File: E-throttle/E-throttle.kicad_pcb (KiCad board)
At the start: 2 copper layers, 100 x 100 mm, 62 parts, among them IC1 BTS441TG, J3 Conn_01x11, J4 Conn_01x11, J5 776087-1, J9 Micro_SD_Card, Q1 NMOS, SW1 SW_Push, U1 74HC123, U2 LM317_SOT-223, U3 LM317_SOT-223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

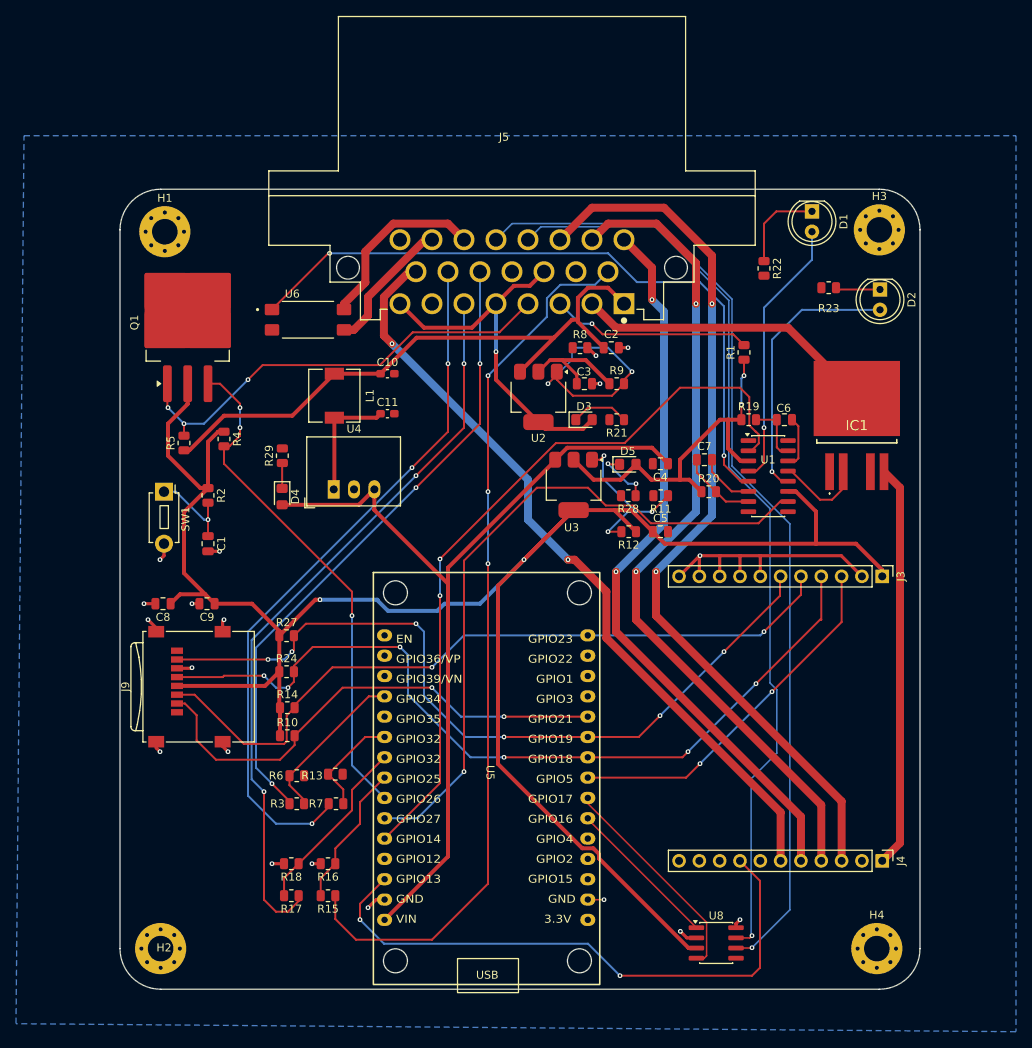
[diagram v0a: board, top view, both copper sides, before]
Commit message: added vias, ran DRC
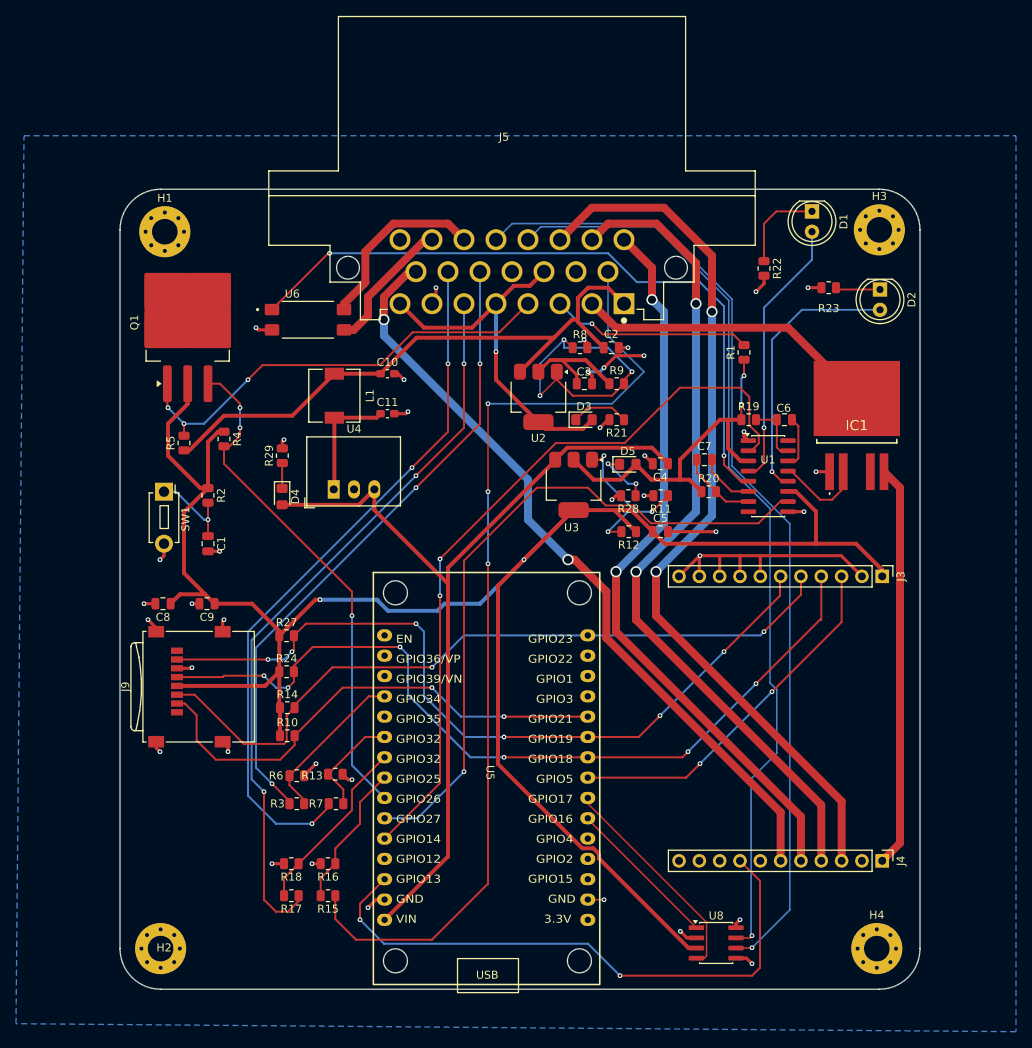
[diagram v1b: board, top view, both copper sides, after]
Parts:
- R13, R16, R18, R6: value 66.5k -> 68k
- R15, R17, R3, R7: value 33.2k -> 33k
- R19: value 10k -> 68k
- R20: value 100k -> 330k
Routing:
- net GND: track 61.9 -> 106.6 mm, vias 18 -> 38
- net /TPS-SIG2: track 111.2 -> 121.5 mm
- net Net-(U2-ADJ): track 29.2 -> 37.1 mm, vias 2 -> 3

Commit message: Added THT filtering capacitors
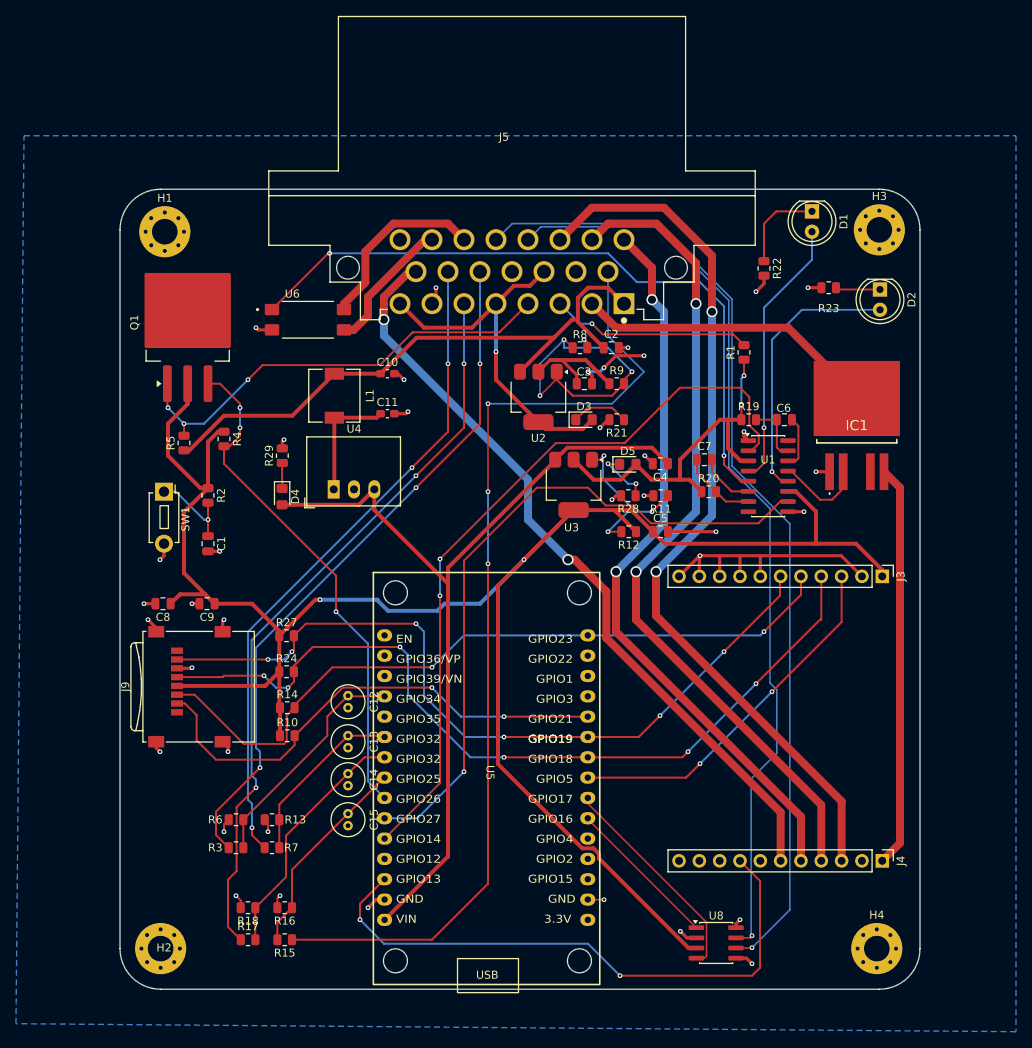
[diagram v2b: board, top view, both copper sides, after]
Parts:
- added C12: 0.1u, Capacitor_THT:C_Radial_D4.0mm_H7.0mm_P1.50mm, F.Cu at (183.2, 96.8)
- added C13: 0.1u, Capacitor_THT:C_Radial_D4.0mm_H7.0mm_P1.50mm, F.Cu at (183.2, 101.8)
- added C14: 0.1u, Capacitor_THT:C_Radial_D4.0mm_H7.0mm_P1.50mm, F.Cu at (183.2, 106.6)
- added C15: 0.1u, Capacitor_THT:C_Radial_D4.0mm_H7.0mm_P1.50mm, F.Cu at (183.2, 111.6)
- R16, R18: value 68k -> 100k
- moved R13 9.75 mm to (173.7, 112.3), turned to 180 degrees
- moved R7 9.71 mm to (173.7, 115.8)
- moved R3 9.38 mm to (169.2, 115.8)
- moved R6 9.38 mm to (169.2, 112.3), turned to 180 degrees
- moved R15 7.72 mm to (175.3, 127.3)
- moved R16 7.72 mm to (175.3, 123.3)
- moved R17 7.72 mm to (170.7, 127.3), turned to 0 degrees
- moved R18 7.72 mm to (170.7, 123.3)
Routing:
- net /APPS-SIG1-OUT: track 20.3 -> 29.0 mm
- net /APPS-SIG2-OUT: track 13.5 -> 22.2 mm
- net /TPS-SIG1-OUT: track 22.5 -> 31.0 mm
- net /TPS-SIG2-OUT: track 18.1 -> 25.8 mm
- net /APPS-SIG1: track 79.8 -> 86.7 mm
- net /APPS-SIG2: track 88.7 -> 83.2 mm
- net /TPS-SIG2: track 121.5 -> 122.9 mm
- net GND: track 106.6 -> 107.3 mm
- net /TPS-SIG1: track 92.3 -> 92.8 mm

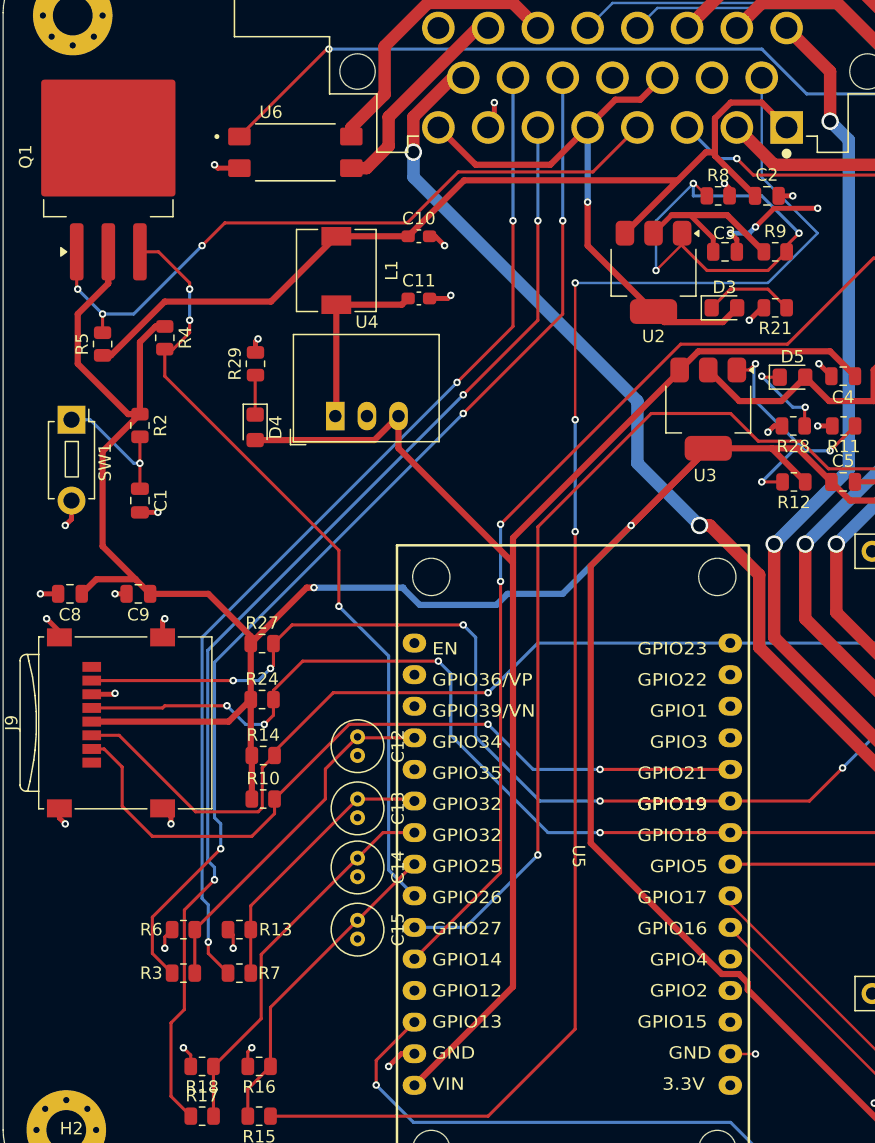
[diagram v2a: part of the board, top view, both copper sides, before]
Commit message: Added FBR Logo
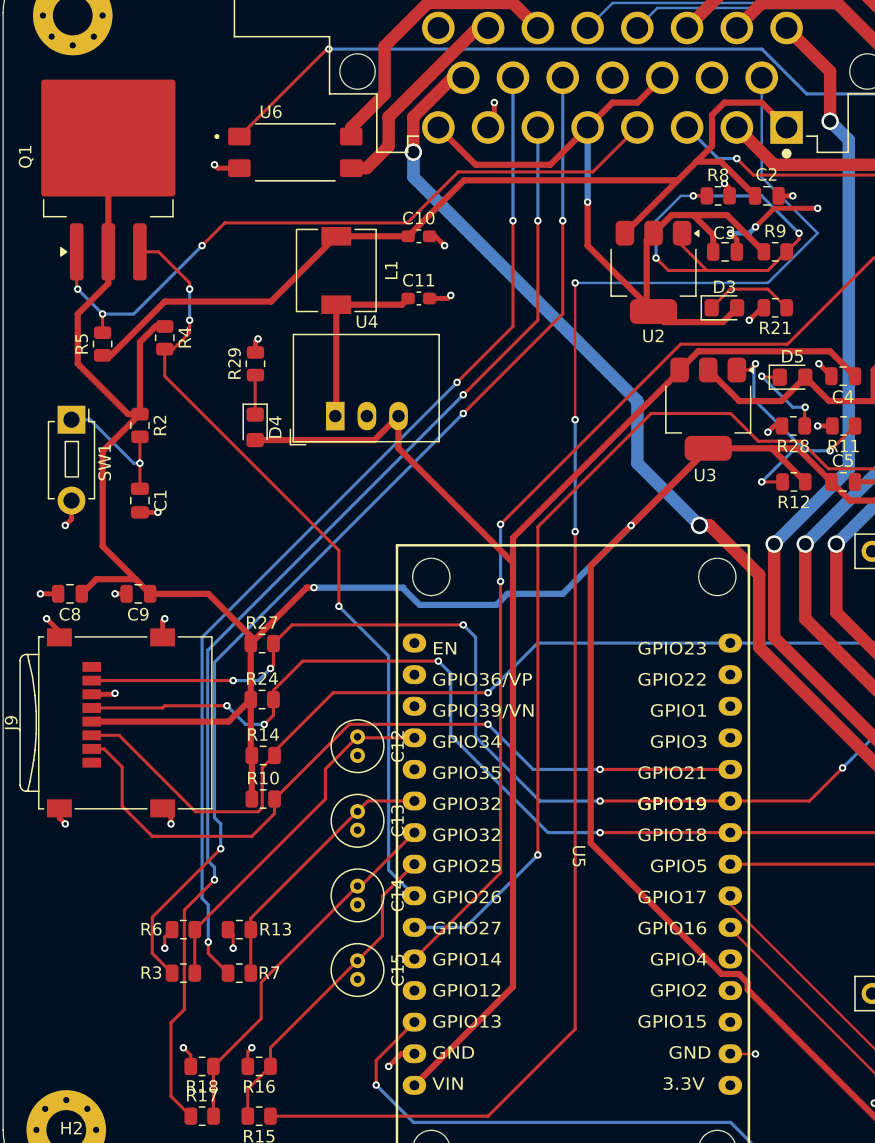
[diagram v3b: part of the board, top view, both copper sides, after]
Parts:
- added E-Throttle (2026): LOGO, FBR_Footprints_additional:FBR_Logo_.9in, B.Cu at (242.5, 60.0)
- moved C15 3.25 mm to (183.2, 114.8)
- moved C14 2.25 mm to (183.2, 108.8)
- moved C13 1.00 mm to (183.2, 102.8)
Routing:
- net +3V3: track 298.8 -> 307.9 mm
- net +5V-SENSORS: track 62.6 -> 67.8 mm
- net Net-(U2-ADJ): track 37.1 -> 35.4 mm
- net /TPS-SIG1-OUT: track 31.0 -> 29.7 mm
- net +12V: track 76.7 -> 77.6 mm

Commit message: Ran DRC - fixed all errors
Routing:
- net GND: track 107.3 -> 111.4 mm, vias 38 -> 39
- net +3V3: track 307.9 -> 310.1 mm
- net /CAN-L: vias 1 -> 3
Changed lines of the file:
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@@
 	)
 	(segment
+		(start 234.76 117.46)
+		(end 232.12 114.82)
+		(width 0.25)
+		(layer "F.Cu")
+		(net 1)
+	)
+	(segment
 		(start 229.68 81.9)
 		(end 229.68 79.36)
@@
 	)
 	(segment
+		(start 232.12 114.82)
+		(end 231.72 114.82)
+		(width 0.25)
+		(layer "F.Cu")
+		(net 1)
+	)
+	(segment
 		(start 221.395 71.82)
 		(end 220.22 71.82)
@@
 	)
 	(via
+		(at 231.72 114.82)
+		(size 0.6)
+		(drill 0.3)
+		(layers "F.Cu" "B.Cu")
+		(net 1)
+	)
+	(via
 		(at 163.72 93.32)
 		(size 0.6)
@@
 	)
 	(segment
+		(start 239.68 71.28)
+		(end 246.22 77.82)
+		(width 0.4)
+		(layer "F.Cu")
+		(net 5)
+	)
+	(segment
 		(start 233.27 67.47)
 		(end 232.295001 67.47)
@@
 	)
 	(segment
-		(start 246.72 77.82)
+		(start 246.22 77.82)
 		(end 241.72 77.82)
 		(width 0.5)
@@
 	)
 	(segment
-		(start 238.22 71.28)
-		(end 239.194999 71.28)
-		(width 0.5)
-		(layer "F.Cu")
-		(net 5)
-	)
-	(segment
 		(start 217.3 69.82)
 		(end 219.22 67.9)
@@
 	)
 	(segment
+		(start 238.22 71.28)
+		(end 239.68 71.28)
+		(width 0.4)
+		(layer "F.Cu")
+		(net 5)
+	)
+	(segment
 		(start 225.795001 128.36)
 		(end 214.59246 117.157459)
@@
 	)
 	(segment
-		(start 241.72 73.805001)
-		(end 241.72 77.82)
-		(width 0.5)
-		(layer "F.Cu")
-		(net 5)
-	)
-	(segment
 		(start 216.52 73.62)
 		(end 219.22 76.32)
@@
 	)
 	(segment
-		(start 239.194999 71.28)
-		(end 241.72 73.805001)
+		(start 246.72 77.82)
+		(end 246.22 77.82)
 		(width 0.5)
 		(layer "F.Cu")
@@
 	)
 	(segment
+		(start 238.45 123.59)
+		(end 236.72 125.32)
+		(width 0.2)
+		(layer "F.Cu")
+		(net 41)
+	)
+	(segment
+		(start 238.45 121.32)
+		(end 238.45 123.59)
+		(width 0.2)
+		(layer "F.Cu")
+		(net 41)
+	)
+	(segment
 		(start 233.68 128.36)
 		(end 233.72 128.32)
@@
 	)
 	(via
+		(at 238.45 121.32)
+		(size 0.6)
+		(drill 0.3)
+		(layers "F.Cu" "B.Cu")
+		(net 41)
+	)
+	(via
 		(at 233.72 128.32)
 		(size 0.6)
@@
 		(net 41)
 	)
+	(via
+		(at 236.72 125.32)
+		(size 0.6)
+		(drill 0.3)
+		(layers "F.Cu" "B.Cu")
+		(net 41)
+	)
 	(segment
 		(start 238.45 75.332843)
@@
 	(segment
 		(start 233.72 128.32)
-		(end 238.45 123.59)
+		(end 236.72 125.32)
 		(width 0.2)
 		(layer "B.Cu")
@@
 	)
 	(segment
-		(start 231.22 47.244085)
-		(end 221.783414 37.8075)
+		(start 238.45 121.32)
+		(end 238.45 75.332843)
 		(width 0.2)
 		(layer "B.Cu")
@@
 	)
 	(segment
-		(start 238.45 123.59)
-		(end 238.45 75.332843)
+		(start 231.22 47.244085)
+		(end 221.783414 37.8075)
 		(width 0.2)
 		(layer "B.Cu")

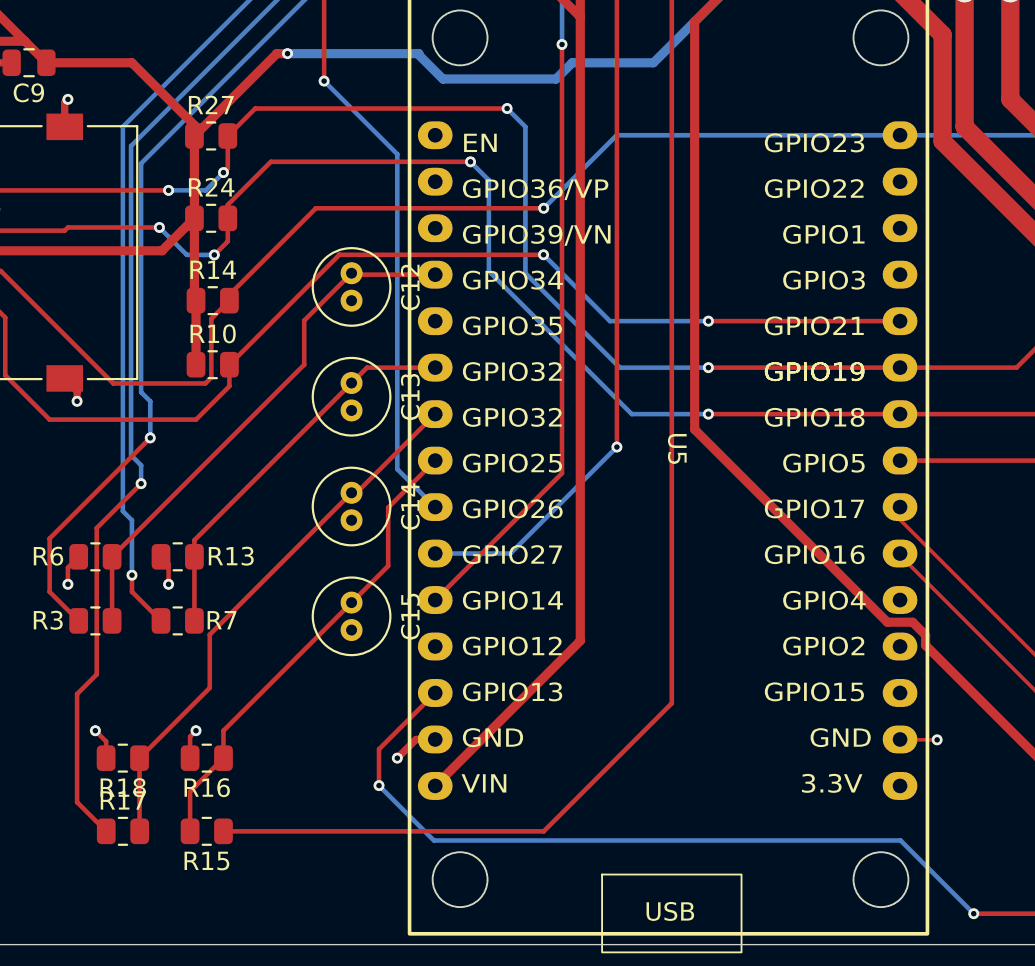
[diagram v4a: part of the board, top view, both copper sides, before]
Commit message: Added Pin Sockets on top of ESP32 Dev Board footprint
Set ESP32 Dev board to be a ghost footprint (not included in BOM, coordinates, etc)

Added 2 1x15 female pin headers to the schematic, assigned them footprints, and aligned the precisely over the U5 pads using magnetic snapping to guarantee 25.4mm pitch
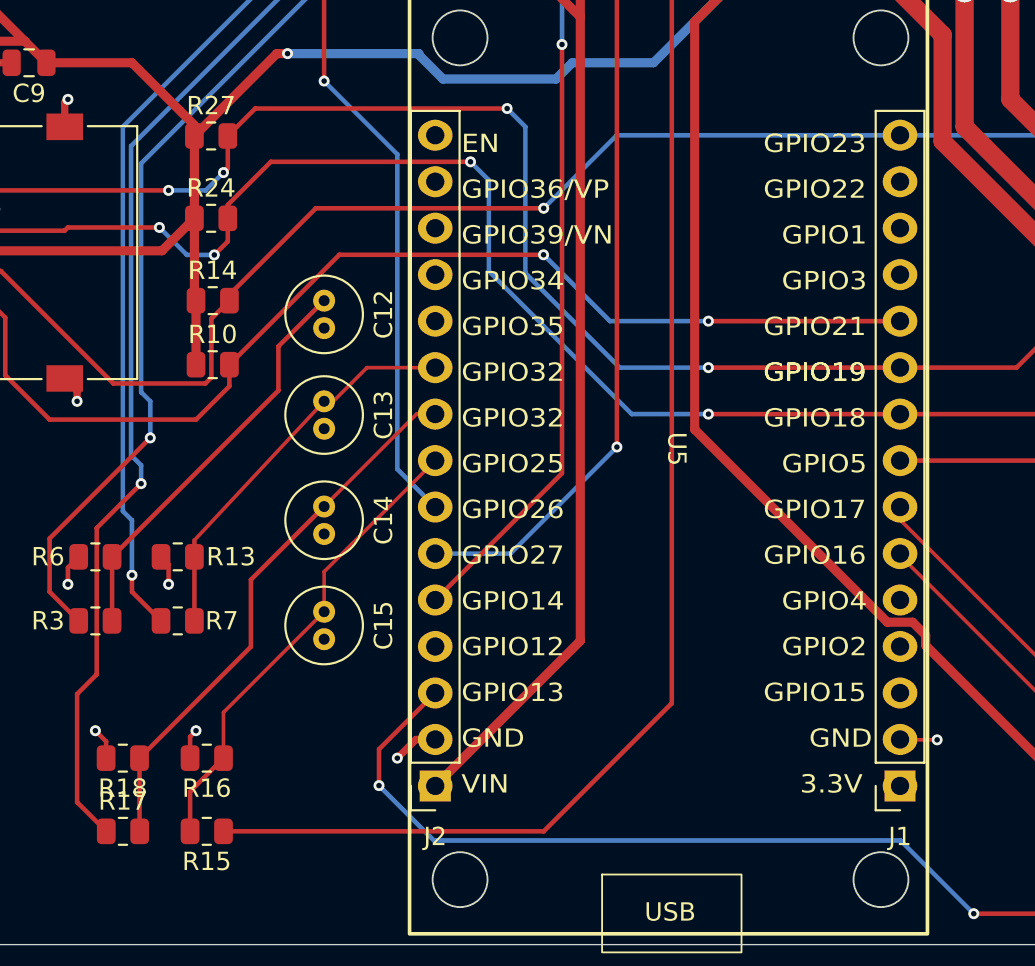
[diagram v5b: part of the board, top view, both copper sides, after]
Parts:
- added J1: Conn_01x15_Socket, Connector_PinSocket_2.54mm:PinSocket_1x15_P2.54mm_Vertical, F.Cu at (213.2, 124.8)
- added J2: Conn_01x15_Socket, Connector_PinSocket_2.54mm:PinSocket_1x15_P2.54mm_Vertical, F.Cu at (187.8, 124.8)
- moved C12 2.12 mm to (181.7, 98.3)
- moved C13 1.80 mm to (181.7, 103.8)
- moved C14 1.68 mm to (181.7, 109.6)
- moved C15 1.58 mm to (181.7, 115.3)
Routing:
- net /APPS-SIG2-OUT: track 21.7 -> 11.5 mm
- net /APPS-SIG1-OUT: track 29.0 -> 22.3 mm
